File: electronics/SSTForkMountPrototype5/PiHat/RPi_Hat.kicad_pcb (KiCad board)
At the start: 4 copper layers, 81.8 x 56 mm, 37 parts, among them CON1 BARREL_JACK, J1 RJ12, J2 RPi_GPIO, J4 Screw_Terminal_01x08, J5 Screw_Terminal_01x03, Q1 Q_NPN_BEC, Q2 Q_NPN_BEC, Q3 Q_NPN_BEC, SW1 SW_SPST, U1 MCQ9435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

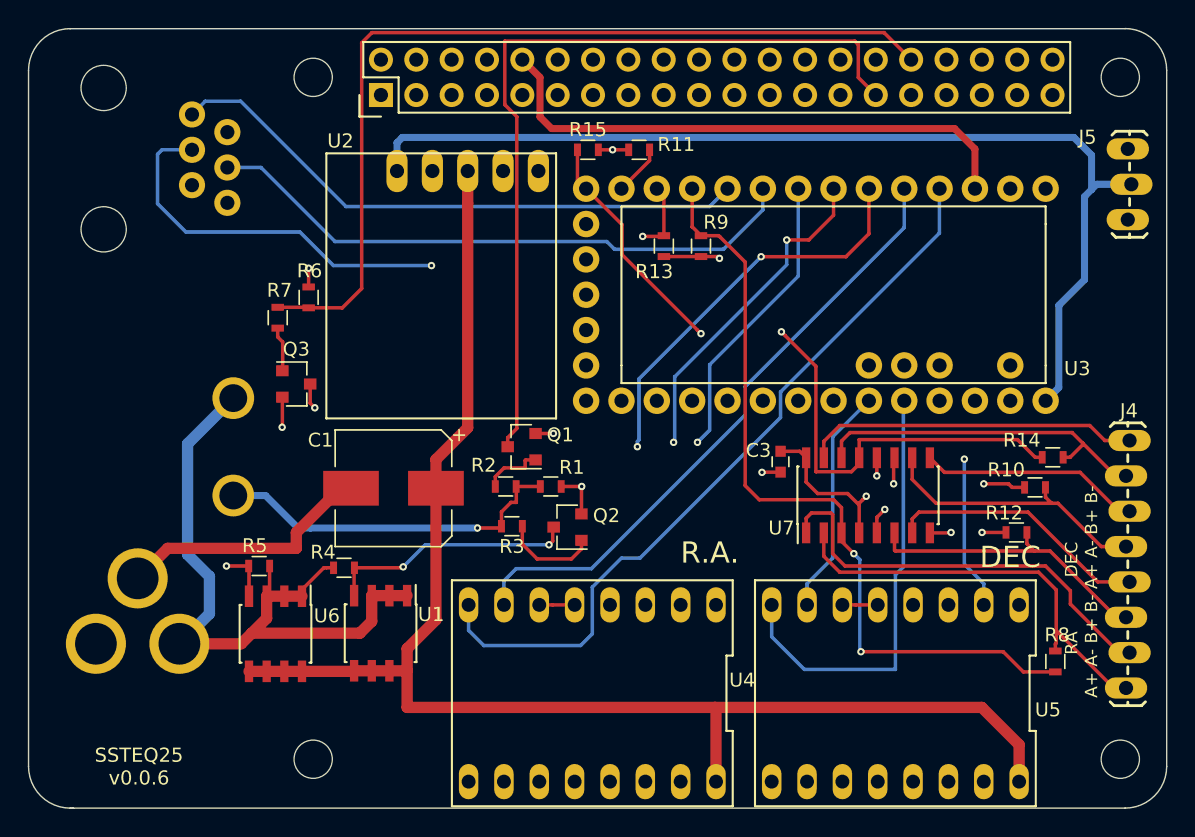
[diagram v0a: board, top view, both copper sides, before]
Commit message: Removed mosfet switching. Seperate DEC/RA encoder headers.
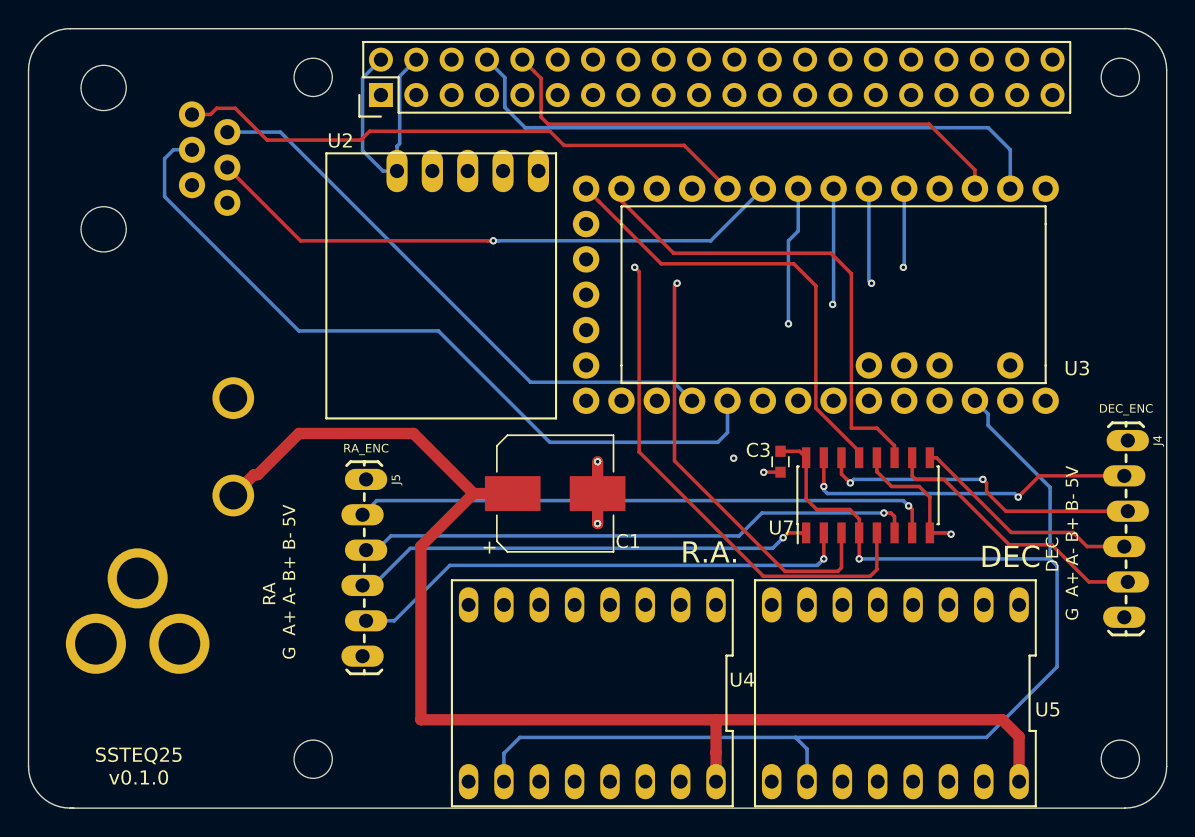
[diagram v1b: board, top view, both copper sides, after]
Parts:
- removed Q1, Q2, Q3: Q_NPN_BEC, TO_SOT_Packages_SMD:SOT-23
- removed R1, R6: 1M, Resistors_SMD:R_0603
- removed R10, R12, R14, R4, R5, R7, R8: 10k, Resistors_SMD:R_0603
- removed R11, R13, R15, R9: 20k, Resistors_SMD:R_0603
- removed R2, R3: 100k, Resistors_SMD:R_0603
- removed U1, U6: MCQ9435, Housings_SOIC:SOIC-8_3.9x4.9mm_Pitch1.27mm
- J4: value Screw_Terminal_01x08 -> DEC_ENC; footprint Connectors:1X08_LOCK_LONGPADS -> Connectors:1X06_LOCK_LONGPADS
- J5: value Screw_Terminal_01x03 -> RA_ENC; footprint Connectors:1X03_LOCK_LONGPADS -> Connectors:1X06_LOCK_LONGPADS
- moved J5 57.8 mm to (123.1, 98.4), turned to 270 degrees
- moved C1 11.6 mm to (136.7, 99.4), turned to 0 degrees
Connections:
- J2 pad 29: PWR_SW_PI -> (no net)
- J2 pad 32: PWR_RELAY_PI -> (no net)
- J4 pad 1: DEC_ENC_B- -> +5V
- J4 pad 2: DEC_ENC_B+ -> DEC_ENC_B-
- J4 pad 3: DEC_ENC_A- -> DEC_ENC_B+
- J4 pad 4: DEC_ENC_A+ -> DEC_ENC_A-
- J4 pad 5: RA_ENC_B- -> DEC_ENC_A+
- J4 pad 6: RA_ENC_B+ -> GND
- J5 pad 1: GND -> +5V
- J5 pad 2: +5V -> RA_ENC_B-
- J5 pad 3: +3V3 -> RA_ENC_B+
- SW1 pad 2: Net-(R1-Pad1) -> +12C
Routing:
- net PWR_RELAY_PI: track 64.9 -> 0.00 mm
- net PWR_SW_PI: track 59.4 -> 0.00 mm
- net +5V: track 93.2 -> 122.7 mm
- net +12V: track 50.7 -> 24.7 mm
- net Net-(R1-Pad1): track 25.6 -> 0.00 mm, vias 1 -> 0
- net RA_ENC_B-: track 18.9 -> 41.9 mm, vias 0 -> 1
- net GND: track 67.1 -> 44.4 mm, vias 9 -> 4
- net DEC_DIR: track 31.7 -> 53.5 mm
- net Net-(Q3-Pad3): track 19.9 -> 0.00 mm, vias 2 -> 0
- net +3V3: track 116.7 -> 97.0 mm
- net DEC_ENC_B: track 52.6 -> 33.0 mm, vias 2 -> 0
- net RA_ENC_B+: track 21.4 -> 40.8 mm, vias 0 -> 1
- net RA_ENC_A: track 56.8 -> 38.0 mm, vias 2 -> 1
- net +12C: track 104.8 -> 123.0 mm
- net Net-(Q2-Pad3): track 18.1 -> 0.00 mm, vias 2 -> 0
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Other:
- board text added: "DEC G A+ A- B+ B- 5V"
- board text added: "RA G A+ A- B+ B- 5V"
- board text added: "SSTEQ25 v0.1.0"
- board text removed: "RA DEC A+ A- B+ B- A+ A- B+ B-"
- board text removed: "SSTEQ25 v0.0.6"

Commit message: Fixed negative inputs. Fixed HADec no tracking status. Fixed infinite slew. Added reverse voltage mosfet.
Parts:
- added Q1: Si2369DS, Package_TO_SOT_SMD:SOT-23, F.Cu at (116.8, 96.3)
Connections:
- J1 pad 1: (no net) -> Net-(J1-Pad1)
- J2 pad 1: (no net) -> Net-(J2-Pad1)
- J2 pad 11: (no net) -> Net-(J2-Pad11)
- J2 pad 12: (no net) -> Net-(J2-Pad12)
- J2 pad 13: (no net) -> Net-(J2-Pad13)
- J2 pad 15: (no net) -> Net-(J2-Pad15)
- J2 pad 16: (no net) -> Net-(J2-Pad16)
- J2 pad 17: (no net) -> Net-(J2-Pad17)
- J2 pad 18: (no net) -> Net-(J2-Pad18)
- J2 pad 19: (no net) -> Net-(J2-Pad19)
- J2 pad 21: (no net) -> Net-(J2-Pad21)
- J2 pad 22: (no net) -> Net-(J2-Pad22)
- J2 pad 23: (no net) -> Net-(J2-Pad23)
- J2 pad 24: (no net) -> Net-(J2-Pad24)
- J2 pad 26: (no net) -> Net-(J2-Pad26)
- J2 pad 27: (no net) -> Net-(J2-Pad27)
- J2 pad 28: (no net) -> Net-(J2-Pad28)
- J2 pad 29: (no net) -> Net-(J2-Pad29)
- J2 pad 3: (no net) -> Net-(J2-Pad3)
- J2 pad 30: (no net) -> Net-(J2-Pad30)
- J2 pad 31: (no net) -> Net-(J2-Pad31)
- J2 pad 32: (no net) -> Net-(J2-Pad32)
- J2 pad 33: (no net) -> Net-(J2-Pad33)
- J2 pad 35: (no net) -> Net-(J2-Pad35)
- J2 pad 36: (no net) -> Net-(J2-Pad36)
- J2 pad 37: (no net) -> Net-(J2-Pad37)
- J2 pad 38: (no net) -> Net-(J2-Pad38)
- J2 pad 40: (no net) -> Net-(J2-Pad40)
- J2 pad 5: (no net) -> Net-(J2-Pad5)
- J2 pad 7: (no net) -> Net-(J2-Pad7)
- SW1 pad 2: +12C -> Net-(Q1-Pad3)
- U2 pad 1: (no net) -> Net-(U2-Pad1)
- U2 pad 2: (no net) -> Net-(U2-Pad2)
- U3 pad 13: (no net) -> Net-(U3-Pad13)
- U3 pad 14: (no net) -> Net-(U3-Pad14)
- U3 pad 15: (no net) -> Net-(U3-Pad15)
- U3 pad 23: (no net) -> Net-(U3-Pad23)
- U3 pad 25: (no net) -> Net-(U3-Pad25)
- U3 pad 28: (no net) -> Net-(U3-Pad28)
- U3 pad 29: (no net) -> Net-(U3-Pad29)
- U3 pad 30: (no net) -> Net-(U3-Pad30)
- U3 pad 31: (no net) -> Net-(U3-Pad31)
- U3 pad 32: (no net) -> Net-(U3-Pad32)
- U3 pad 33: (no net) -> Net-(U3-Pad33)
- U3 pad 34: (no net) -> Net-(U3-Pad34)
- U3 pad 35: (no net) -> Net-(U3-Pad35)
- U3 pad 36: (no net) -> Net-(U3-Pad36)
- U4 pad 1: (no net) -> Net-(U4-Pad1)
- U4 pad 11: (no net) -> Net-(U4-Pad11)
- U4 pad 12: (no net) -> Net-(U4-Pad12)
- U4 pad 13: (no net) -> Net-(U4-Pad13)
- U4 pad 14: (no net) -> Net-(U4-Pad14)
- U5 pad 1: (no net) -> Net-(U5-Pad1)
- U5 pad 11: (no net) -> Net-(U5-Pad11)
- U5 pad 12: (no net) -> Net-(U5-Pad12)
- U5 pad 13: (no net) -> Net-(U5-Pad13)
- U5 pad 14: (no net) -> Net-(U5-Pad14)
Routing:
- net GND: track 44.4 -> 60.7 mm
- net +12C: track 123.0 -> 110.7 mm, vias 0 -> 1
- net Net-(Q1-Pad3): track 0.00 -> 4.27 mm
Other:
- board text added: "3 conn underside"
- board text added: "SSTEQ25 v0.1.1"
- board text removed: "SSTEQ25 v0.1.0"
